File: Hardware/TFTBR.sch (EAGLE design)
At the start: 2 parts, among them J1 SPI-LCD

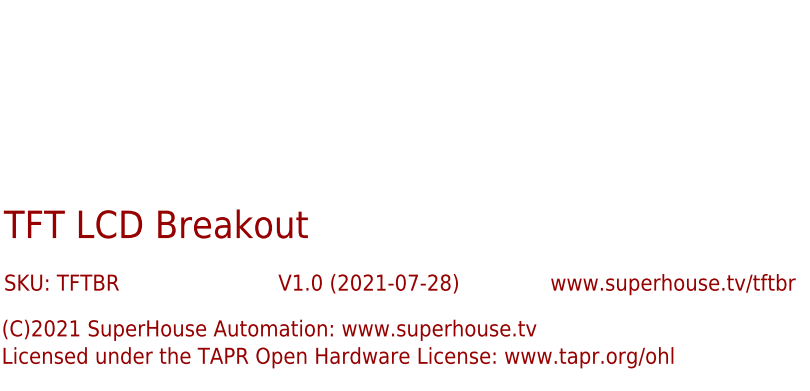
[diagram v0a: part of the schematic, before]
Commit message: Major redesign for v2.0 release.
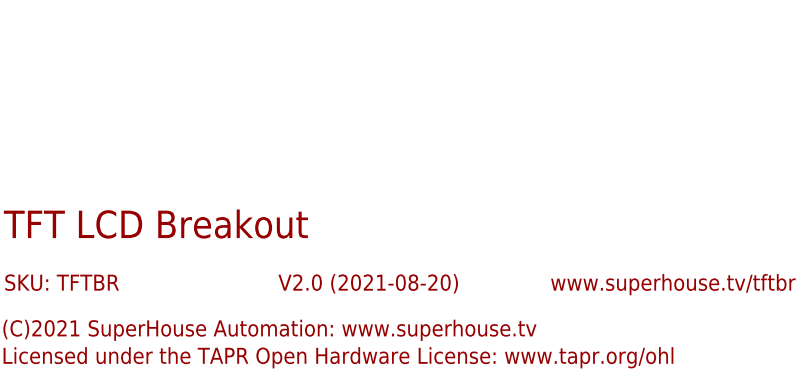
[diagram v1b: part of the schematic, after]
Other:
- note added: "V2.0 (2021-08-20)"
- note removed: "V1.0 (2021-07-28)"
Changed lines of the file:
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@@
 <part name="P+20" library="SuperHouse-SupplySymbols" library_urn="urn:adsk.eagle:library:11790503" deviceset="3.3V" device=""/>
 <part name="GND1" library="SuperHouse-SupplySymbols" library_urn="urn:adsk.eagle:library:11790503" deviceset="GND" device=""/>
-<part name="MOD1" library="SuperHouse-Displays" library_urn="urn:adsk.eagle:library:11966779" deviceset="OLED-SPI-CS" device="-PINS" package3d_urn="urn:adsk.eagle:package:30303932/1"/>
+<part name="MOD1" library="SuperHouse-Displays" library_urn="urn:adsk.eagle:library:11966779" deviceset="OLED-SPI-CS" device="-PINS" package3d_urn="urn:adsk.eagle:package:30303932/2"/>
 </parts>
 <sheets>
@@
 <frame x1="35.56" y1="12.7" x2="66.04" y2="17.78" columns="8" rows="5" layer="94"/>
 <frame x1="5.08" y1="5.08" x2="109.22" y2="17.78" columns="0" rows="0" layer="94" border-left="no" border-top="no" border-right="no" border-bottom="no"/>
-<text x="38.1" y="14.478" size="1.778" layer="94">V1.0 (2021-07-28)</text>
+<text x="38.1" y="14.478" size="1.778" layer="94">V2.0 (2021-08-20)</text>
 <wire x1="99.06" y1="81.28" x2="99.06" y2="132.08" width="0.4064" layer="97" style="longdash"/>
 <wire x1="27.94" y1="81.28" x2="99.06" y2="81.28" width="0.4064" layer="97" style="longdash"/>
